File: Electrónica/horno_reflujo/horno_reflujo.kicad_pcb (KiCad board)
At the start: 2 copper layers, 42 parts, among them J1 LevelShifter, J10 ssr1, J11 ssr2, J12 encoder, J13 Max6675_modulo2, J14 Max6675_modulo3, J15 Max6675_modulo4, J2 LevelShifter, J3 Display Oled I2C, J4 Max6675_modulo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

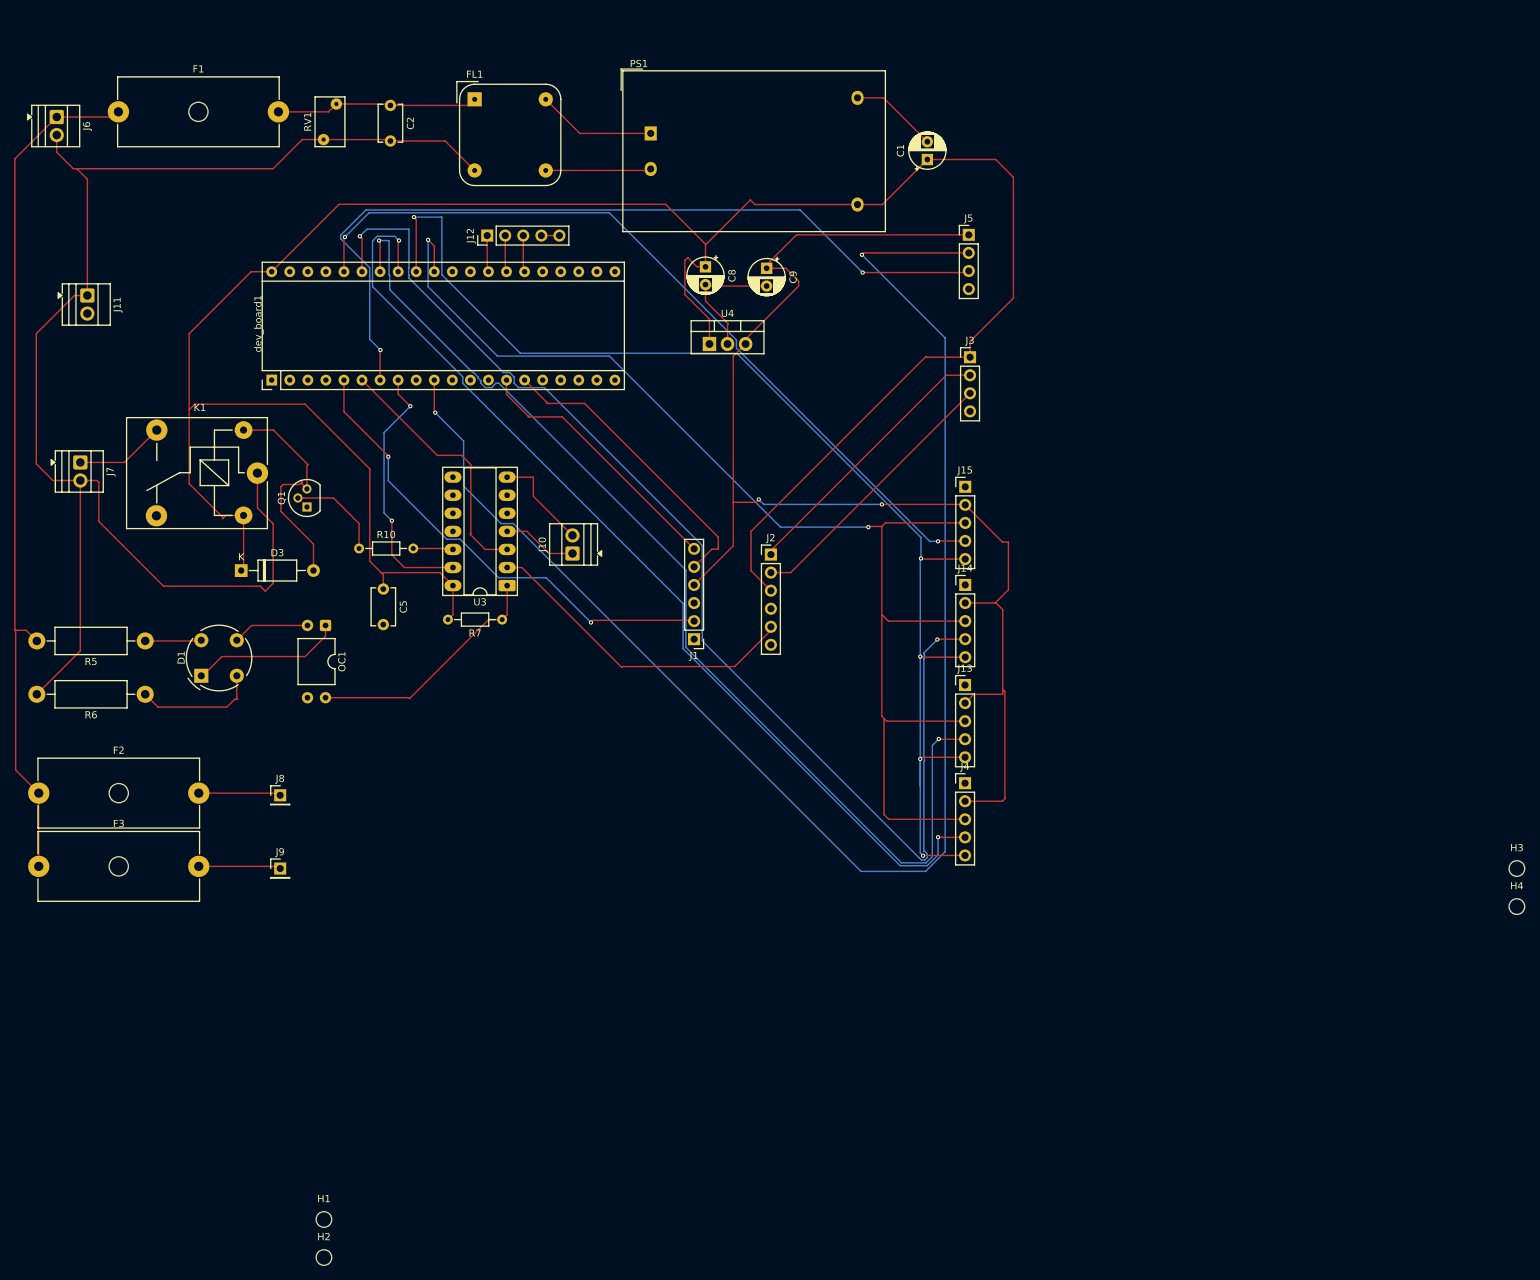
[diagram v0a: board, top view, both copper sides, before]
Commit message: redesigned pcb
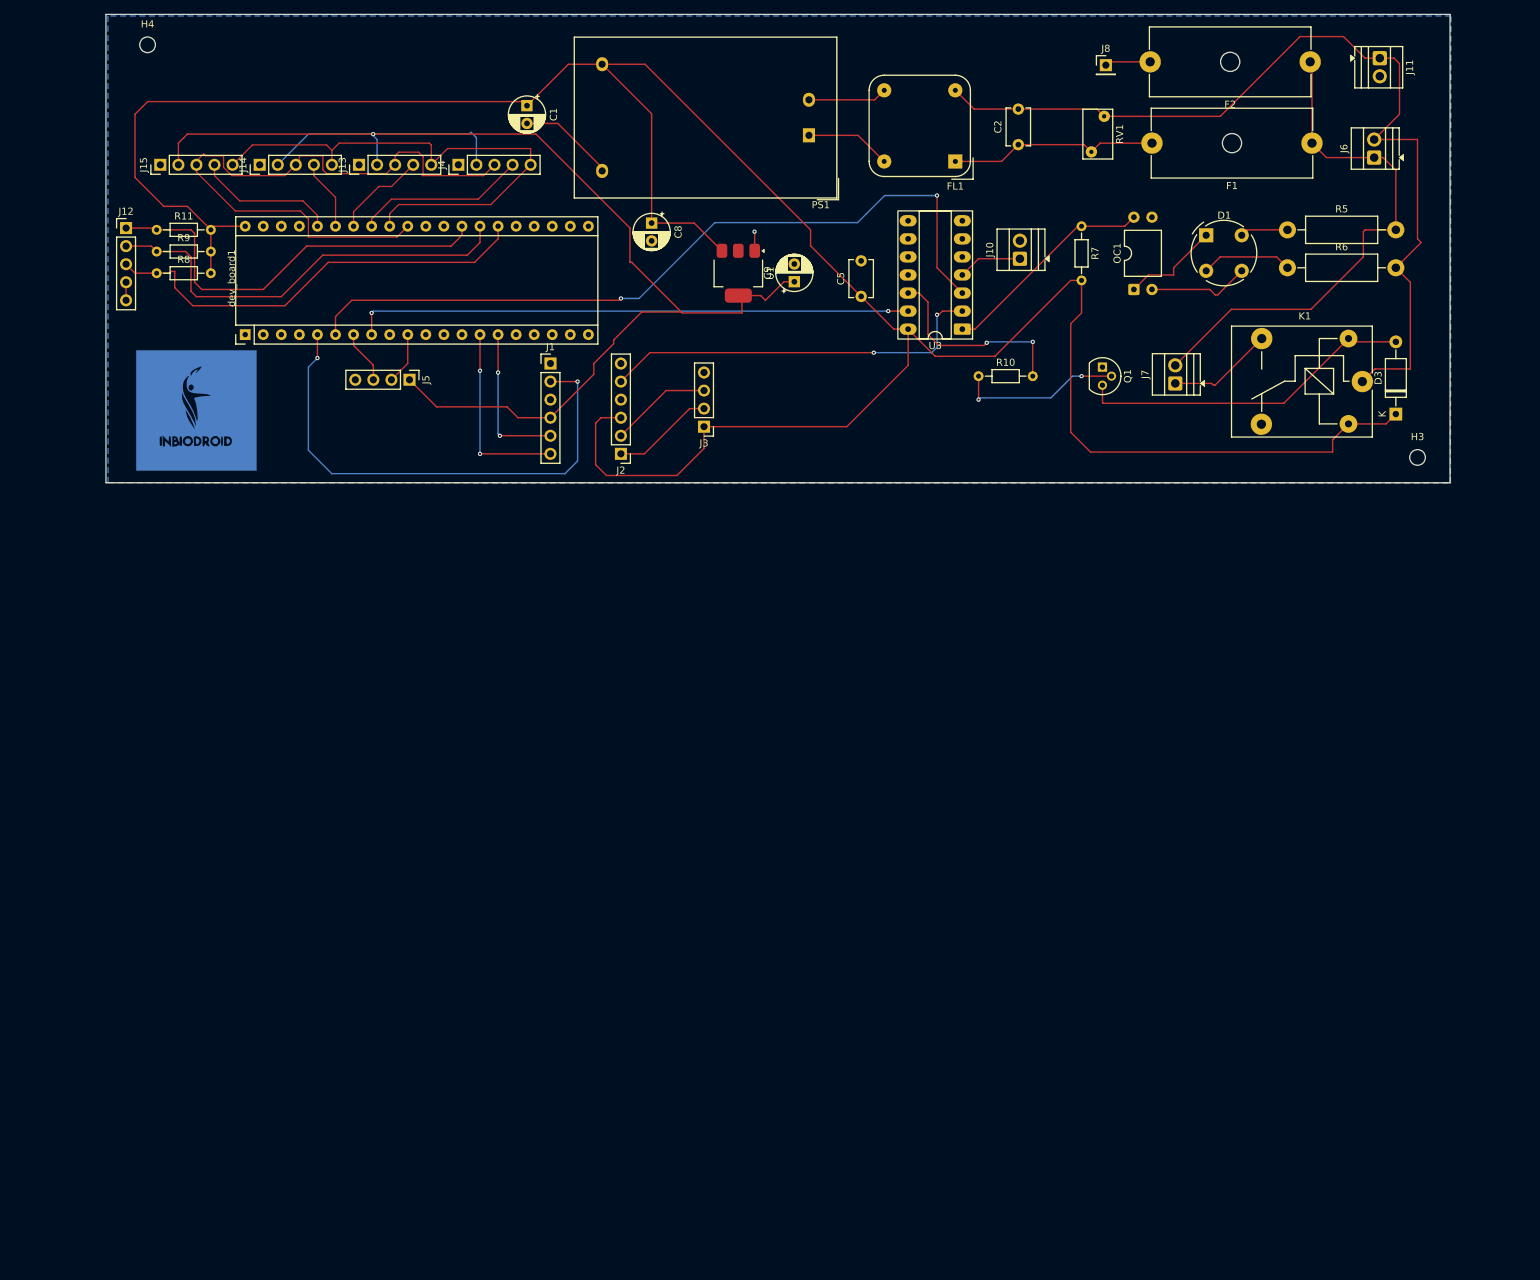
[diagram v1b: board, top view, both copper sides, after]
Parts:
- removed F3: 15A, Fuse:Fuseholder_Cylinder-5x20mm_Schurter_0031_8201_Horizontal_Open
- removed H1, H2: MountingHole, MountingHole:MountingHole_2.2mm_M2_DIN965
- removed J9: resistencia1, Connector_PinHeader_2.54mm:PinHeader_1x01_P2.54mm_Vertical
- removed U4: LM7833CT, Package_TO_SOT_THT:TO-220-3_Vertical
- added G***: LOGO, LOGO, B.Cu at (42.4, 79.0)
- added R11: 10K, Resistor_THT:R_Axial_DIN0204_L3.6mm_D1.6mm_P7.62mm_Horizontal, F.Cu at (36.8, 53.6)
- added R8: 10K, Resistor_THT:R_Axial_DIN0204_L3.6mm_D1.6mm_P7.62mm_Horizontal, F.Cu at (36.8, 59.7)
- added R9: 10K, Resistor_THT:R_Axial_DIN0204_L3.6mm_D1.6mm_P7.62mm_Horizontal, F.Cu at (36.8, 56.6)
- added U1: LD1117S33TR_SOT223, Package_TO_SOT_SMD:SOT-223-3_TabPin2, F.Cu at (118.6, 59.7)
- moved H4 227.5 mm to (35.5, 27.6)
- moved F2 206.2 mm to (199.0, 30.0), turned to 180 degrees
- moved J6 185.3 mm to (208.0, 43.4), turned to 90 degrees
- moved J11 184.8 mm to (208.8, 29.5)
- moved R6 171.4 mm to (195.8, 58.9), turned to 0 degrees
- moved R5 170.7 mm to (195.8, 53.6), turned to 0 degrees
- moved F1 167.9 mm to (199.3, 41.4), turned to 180 degrees
- moved D3 163.8 mm to (211.1, 79.5), turned to 90 degrees
- moved K1 155.9 mm to (206.4, 74.9)
- moved J8 155.0 mm to (170.3, 30.4)
- moved J7 154.4 mm to (180.1, 75.2), turned to 90 degrees
- moved D1 154.3 mm to (184.4, 54.4), turned to 0 degrees
- moved OC1 123.1 mm to (174.2, 62.0), turned to 90 degrees
- moved J15 121.9 mm to (37.3, 44.5), turned to 90 degrees
- moved J14 115.5 mm to (51.3, 44.5), turned to 90 degrees
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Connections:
- J7 pad 2: NEUT -> LINE
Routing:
- net /Rx_mcu_esp01: track 211.8 -> 7.30 mm, vias 2 -> 0
- net CS_2: track 170.5 -> 9.90 mm, vias 2 -> 0
- net CS_1: track 150.6 -> 13.5 mm, vias 2 -> 0
- net CS_0: track 139.5 -> 24.0 mm, vias 2 -> 0
- net /Tx_mcu_esp01: track 116.2 -> 7.51 mm, vias 2 -> 0
- net SPI1_MISO: track 176.2 -> 76.4 mm, vias 5 -> 0
- net CS_3: track 113.4 -> 19.8 mm, vias 2 -> 0
- net SPI1_SCK: track 177.1 -> 91.2 mm, vias 2 -> 0
- net NEUT: track 205.2 -> 130.7 mm
- net /fire: track 36.2 -> 109.4 mm, vias 0 -> 2
- net ENCODER_A: track 5.16 -> 61.9 mm
- net ENCODER_B: track 5.16 -> 61.0 mm
- net ENCODER_BTN: track 5.16 -> 59.2 mm
- net LINE: track 122.0 -> 74.3 mm
- net /fan: track 36.6 -> 78.6 mm
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- added copper zone on B.Cu, net GND
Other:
- board outline added: 189 x 65.9 mm

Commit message: final check
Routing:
- net GND: track 18.8 -> 17.8 mm
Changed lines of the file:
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@@
 			(outputformat 1)
 			(mirror no)
-			(drillshape 1)
+			(drillshape 0)
 			(scaleselection 1)
-			(outputdirectory "")
+			(outputdirectory "../output/")
 		)
 	)
@@
 	)
 	(segment
-		(start 32.526 60.962)
-		(end 32.526 63.502)
+		(start 120.918 54.878)
+		(end 120.904 54.864)
 		(width 0.2)
 		(layer "F.Cu")
@@
 	)
 	(segment
-		(start 99.4685 44.8585)
-		(end 93.242888 38.632888)
+		(start 32.526 60.962)
+		(end 32.526 63.502)
 		(width 0.2)
 		(layer "F.Cu")
@@
 	)
 	(segment
-		(start 93.242888 38.632888)
-		(end 88.9 38.632888)
+		(start 120.918 56.54)
+		(end 120.918 54.878)
 		(width 0.2)
 		(layer "F.Cu")
@@
 	)
 	(segment
-		(start 120.918 53.862)
-		(end 120.904 53.848)
+		(start 99.4685 44.8585)
+		(end 93.242888 38.632888)
 		(width 0.2)
 		(layer "F.Cu")
@@
 	)
 	(segment
-		(start 120.918 56.54)
-		(end 120.918 53.862)
+		(start 93.242888 38.632888)
+		(end 88.9 38.632888)
 		(width 0.2)
 		(layer "F.Cu")
@@
 	)
 	(via
-		(at 120.904 53.848)
+		(at 120.904 54.864)
 		(size 0.6)
 		(drill 0.3)

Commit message: reorganizacion de folders
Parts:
- removed the G*** at (42.4, 79.0)
- removed U3: 74LS14, Package_DIP:DIP-14_W7.62mm_Socket_LongPads
- added G***: LOGO, LOGO, F.Cu at (97.5, 74.9)
- added G***: LOGO, LOGO, F.Cu at (78.8, 73.3)
- added G***: LOGO, LOGO, F.Cu at (42.5, 94.2)
- added H1: MountingHole, MountingHole:MountingHole_3.2mm_M3_DIN965, F.Cu at (39.5, 30.7)
- added H2: MountingHole, MountingHole:MountingHole_3.2mm_M3_DIN965, F.Cu at (38.9, 102.5)
- added U2: 74LS14, Package_DIP:DIP-14_W7.62mm_Socket_LongPads, F.Cu at (68.5, 57.1)
- H3, H4: footprint MountingHole:MountingHole_2.2mm_M2_DIN965 -> MountingHole:MountingHole_3.2mm_M3_DIN965
- J10, J11, J6, J7: footprint TerminalBlock:TerminalBlock_Xinya_XY308-2.54-2P_1x02_P2.54mm_Horizontal -> TerminalBlock:TerminalBlock_bornier-2_P5.08mm
- R10, R11, R7, R8, R9: footprint Resistor_THT:R_Axial_DIN0204_L3.6mm_D1.6mm_P7.62mm_Horizontal -> Resistor_THT:R_Axial_DIN0207_L6.3mm_D2.5mm_P2.54mm_Vertical
- R5, R6: footprint Resistor_THT:R_Axial_DIN0411_L9.9mm_D3.6mm_P15.24mm_Horizontal -> Resistor_THT:R_Axial_DIN0411_L9.9mm_D3.6mm_P5.08mm_Vertical
- moved H4 121.5 mm to (131.2, 102.5), turned to -90 degrees
- moved D3 119.8 mm to (101.0, 32.2), turned to -90 degrees
- moved K1 109.3 mm to (104.3, 35.8), turned to 0 degrees
- moved H3 99.2 mm to (131.8, 30.3), turned to 180 degrees
- moved J6 93.1 mm to (130.9, 95.6)
- moved R6 88.7 mm to (107.9, 47.2)
- moved R5 87.9 mm to (107.9, 51.7)
- moved J11 86.4 mm to (125.5, 52.2), turned to 90 degrees
- moved C9 86.3 mm to (48.7, 98.4)
- moved OC1 82.2 mm to (93.8, 45.1), turned to -90 degrees
- moved D1 80.8 mm to (103.6, 52.0), turned to 180 degrees
- moved Q1 80.5 mm to (96.7, 39.3), turned to 90 degrees
- moved F2 77.6 mm to (133.3, 71.2)
- moved F1 77.2 mm to (133.3, 81.6)
- moved J8 77.2 mm to (104.8, 71.2), turned to 90 degrees
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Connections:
- J13 pad 2: +3.3V -> +3.3Vmc
- J14 pad 2: +3.3V -> +3.3Vmc
- J15 pad 2: +3.3V -> +3.3Vmc
- J4 pad 2: +3.3V -> +3.3Vmc
- J6 pad 1: LINE -> NEUT
- J6 pad 2: NEUT -> LINE
- R5 pad 2: LINE -> Net-(J8-Pin_1)
- dev_board1 pad 38: unconnected-(dev_board1-3.3-Pad38) -> +3.3Vmc
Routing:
- net +5V: track 369.9 -> 219.8 mm
- net +3.3V: track 194.2 -> 57.8 mm, vias 1 -> 0
- net /fire: track 109.4 -> 11.9 mm, vias 2 -> 0
- net LINE: track 74.3 -> 171.3 mm, vias 0 -> 7
- net /Rx_mcu_esp01: track 7.30 -> 89.3 mm
- net zero: track 54.8 -> 133.0 mm, vias 2 -> 0
- net /fan: track 78.6 -> 12.3 mm, vias 2 -> 0
- net +3.3Vmc: track 0.00 -> 58.1 mm
- net NEUT: track 130.7 -> 175.7 mm, vias 0 -> 8
- net /Tx_mcu_esp01: track 7.51 -> 51.9 mm
- net Net-(J10-Pin_1): track 9.04 -> 48.8 mm
- net /zc: track 71.7 -> 38.2 mm, vias 2 -> 0
- net Net-(D3-A): track 47.7 -> 14.7 mm
- net I2C1_SDA: track 21.4 -> 51.7 mm, vias 2 -> 0
- net Net-(J8-Pin_1): track 6.43 -> 28.2 mm
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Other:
- board size 189 x 65.9 mm -> 100 x 80 mm
- board text added: "3.3V"
- board text added: "5v"
- board text added: "CS0"
- board text added: "CS1"
- board text added: "CS2"
- board text added: "CS3"
- board text added: "GND"
- board text added: "LINE VENT"
- board text added: "MISO"
- board text added: "NEUT LINE"
- board text added: "NEUT SSR"
- board text added: "RESISTENCIA"
- board text added: "SCK"
- board text added: "SCL"
- board text added: "SDA"
